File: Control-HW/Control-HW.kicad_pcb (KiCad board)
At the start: 2 copper layers, 52 parts, among them J1 Pins_2.54_1x12, U1 ATMEGA8A-AN, U2 2EDL8024GXUMA1, U3 2EDL8024GXUMA1, U4 2EDL8024GXUMA1, U5 MCP1755T-3302E/OT, U6 AP3015KTR-G1, Y1 CSTNE16M0V530000R0

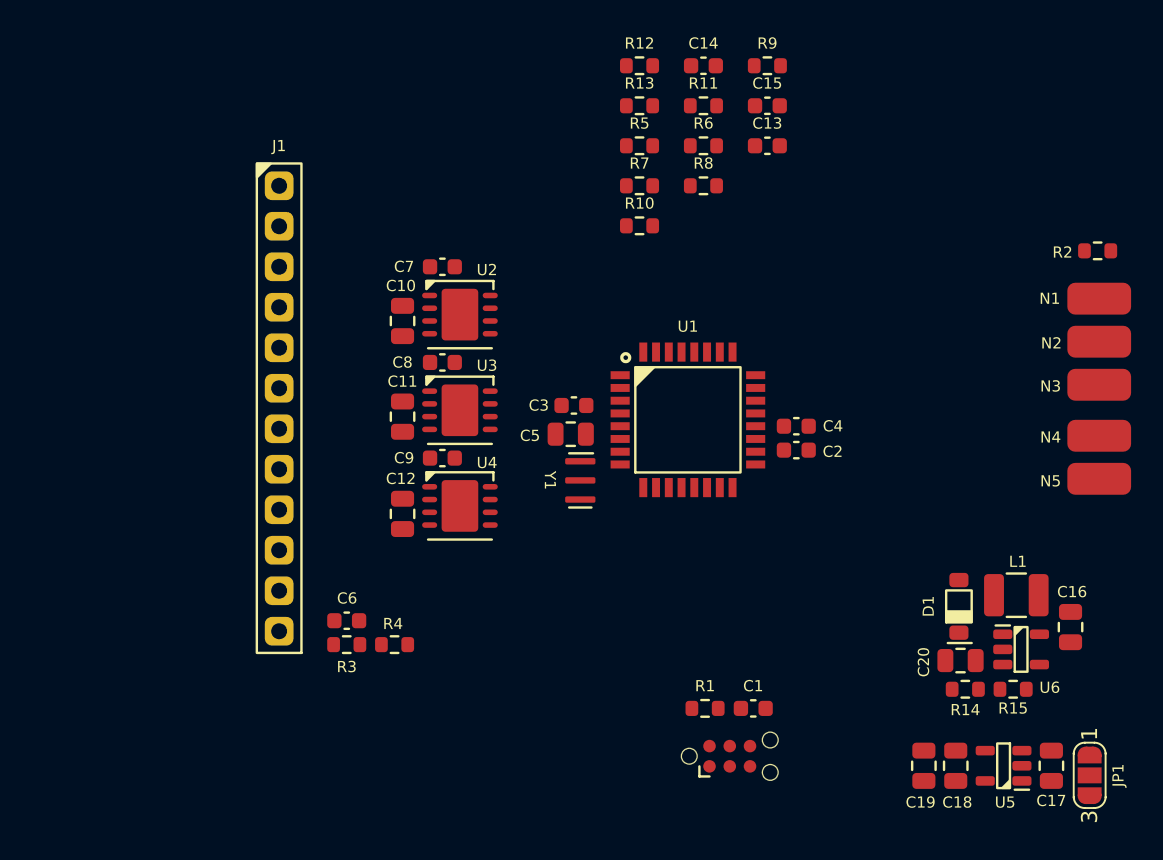
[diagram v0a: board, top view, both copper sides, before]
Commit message: Implemented control pcb
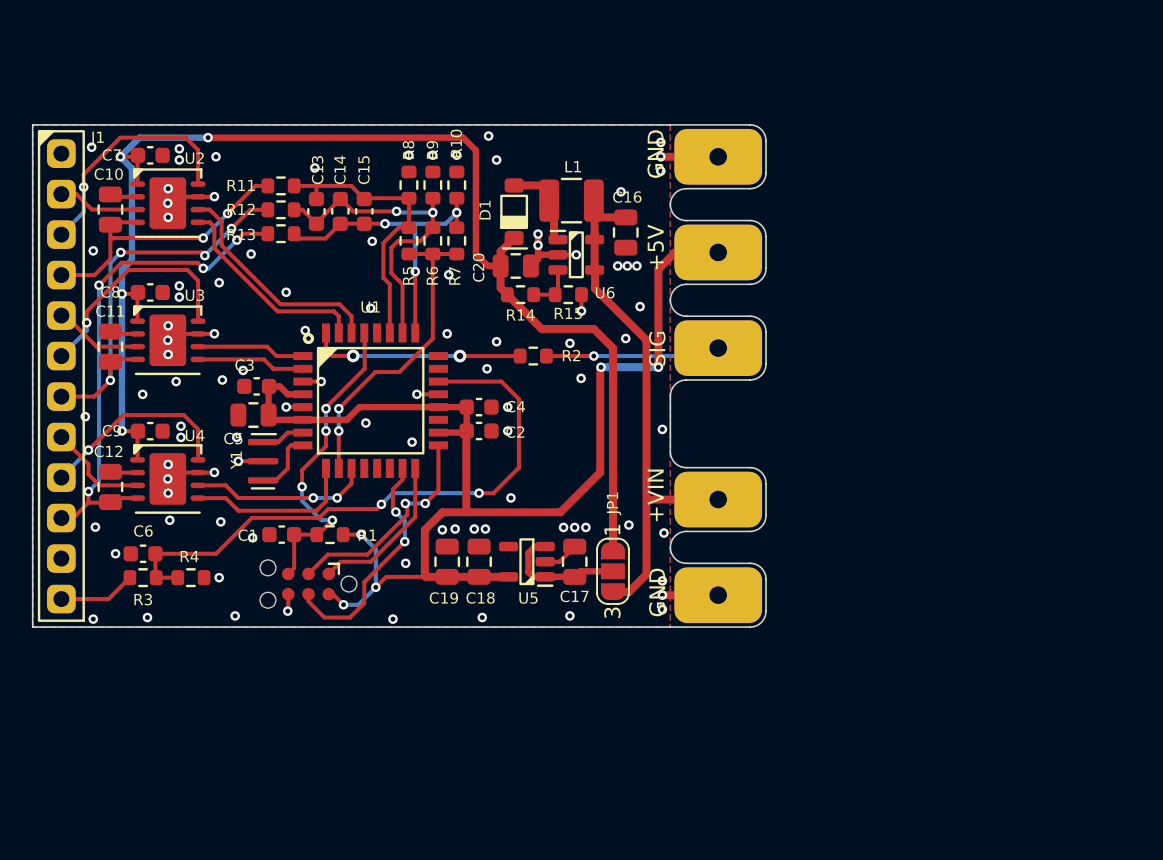
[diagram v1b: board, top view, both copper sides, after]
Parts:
- N1, N2, N3, N4, N5: value Pad_4x2 -> Finger_4x6_M1; footprint N_NonPart:Pad_4x2 -> N_NonPart:Finger_4x6_M1
- moved C16 37.3 mm to (126.4, 92.2)
- moved C20 37.3 mm to (119.5, 94.3)
- moved D1 37.3 mm to (119.4, 91.0)
- moved L1 37.3 mm to (123.0, 90.2)
- moved R14 37.3 mm to (119.8, 96.2)
- moved R15 37.3 mm to (122.8, 96.2)
- moved U6 37.3 mm to (123.3, 93.7)
- moved R2 36.0 mm to (120.6, 100.0)
- moved JP1 32.5 mm to (125.6, 113.5)
- moved C17 32.5 mm to (123.2, 112.9)
- moved C18 32.5 mm to (117.2, 112.9)
- moved C19 32.5 mm to (115.2, 112.9)
- moved U5 32.5 mm to (120.2, 112.9)
- moved C1 31.5 mm to (104.8, 111.2), turned to 180 degrees
- moved C13 28.6 mm to (107.0, 90.9), turned to -90 degrees
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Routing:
- net +12V: track 0.00 -> 82.6 mm, vias 0 -> 4
- net +5V: track 0.00 -> 79.9 mm, vias 0 -> 5
- net /MCU/VBATT_AIN: track 0.00 -> 37.7 mm, vias 0 -> 2
- net /Power/BATT_2S: track 0.00 -> 33.7 mm
- net /Drivers/PHASE_C: track 0.00 -> 31.0 mm, vias 0 -> 4
- net GND: track 0.00 -> 30.5 mm, vias 0 -> 94
- net /Drivers/PHASE_B: track 0.00 -> 25.2 mm, vias 0 -> 4
- net /MCU/SENSE_B: track 0.00 -> 20.9 mm, vias 0 -> 2
- net /MCU/ICSP_NRST: track 0.00 -> 20.0 mm, vias 0 -> 4
- net /MCU/SENSE_COM: track 0.00 -> 19.8 mm, vias 0 -> 2
- net /MCU/SENSE_C: track 0.00 -> 19.7 mm, vias 0 -> 3
- net /Drivers/PHASE_A: track 0.00 -> 18.5 mm, vias 0 -> 2
- net /MCU/SENSE_A: track 0.00 -> 18.4 mm
- net /Drivers/GATE_AL: track 0.00 -> 14.9 mm, vias 0 -> 1
- net /MCU/ICSP_MOSI: track 0.00 -> 14.8 mm, vias 0 -> 2
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- added copper zone on B.Cu, net GND
- added copper zone on F.Cu, net GND
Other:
- board outline added: 46 x 31.5 mm
- board text added: "+5V"
- board text added: "+VIN"
- board text added: "GND"
- board text added: "SIG"

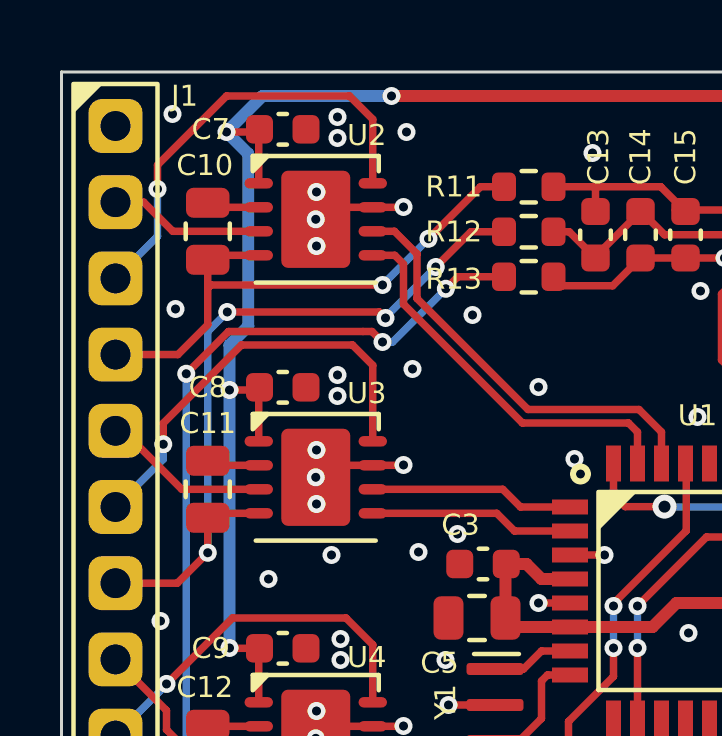
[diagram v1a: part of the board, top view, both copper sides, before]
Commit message: Improve ground path a smidge
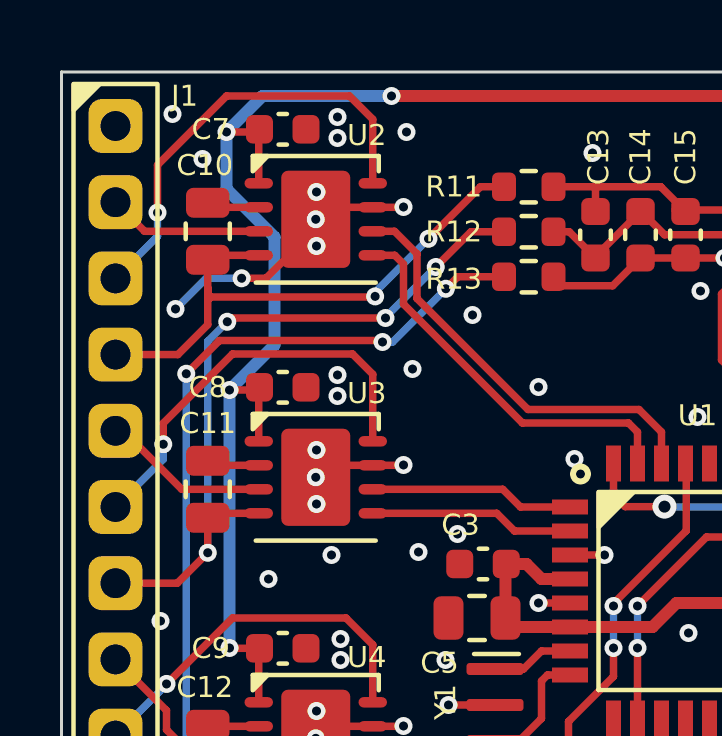
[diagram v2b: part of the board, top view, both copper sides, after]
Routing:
- net GND: track 30.5 -> 34.7 mm, vias 94 -> 96
- net +12V: track 82.6 -> 83.4 mm
- net /Drivers/PHASE_A: track 18.5 -> 19.1 mm
